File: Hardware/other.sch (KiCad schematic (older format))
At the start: 28 parts, among them J10 TILT_OUT, J11 TILT IN, J12 LED EN, J5 DBG, J6 TRACE, J7 I2C INTERNAL, J8 B5B-XH-A__LF__SN_, J9 B8B-XH-A_LF__SN_

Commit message: Add pcb route and ground plane
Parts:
- removed D8: LED_0805, symbol Device:LED_ALT
- removed J10: TILT_OUT, Connector_PinHeader_2.54mm:PinHeader_1x01_P2.54mm_Vertical, symbol Connector:Conn_01x01_Male
- removed J11: TILT IN, Connector_PinHeader_2.54mm:PinHeader_1x01_P2.54mm_Vertical, symbol Connector:Conn_01x01_Male
- removed R70: 1.5K, Resistor_SMD:R_0603_1608Metric, symbol Device:R
- removed S4: POWER, EcoApi_pcb:SW_PUSH, symbol EcoApi_pcb:SW_PUSH
- added J10: TILT, Connector_PinHeader_2.54mm:PinHeader_1x02_P2.54mm_Vertical, symbol Connector:Conn_01x02_Male
- D7: value LED_0805 -> LED_0603_BLUE; footprint (none) -> LED_SMD:LED_0603_1608Metric
- J12: value LED EN -> POWER ON
- J5: footprint (none) -> Connector_PinHeader_2.54mm:PinHeader_1x05_P2.54mm_Vertical
- J6: footprint (none) -> Connector_PinHeader_2.54mm:PinHeader_1x03_P2.54mm_Vertical
- J8: footprint (none) -> EcoApi_pcb:SHDR5W64P0X250_1X5_1490X575X700P
- J9: footprint (none) -> EcoApi_pcb:SHDR8W64P0X250_1X8_2240X575X700P
- S2: footprint (none) -> EcoApi_pcb:DSHP06TSGET
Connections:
- net labels removed: LOADCELL_E-, LOADCELL_SHIELD
- wire segments 81 -> 82
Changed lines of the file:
@@
 Text GLabel 2600 1350 2    50   Input ~ 0
 LOADCELL_E+
-Text GLabel 2600 1450 2    50   Input ~ 0
-LOADCELL_E-
 Text GLabel 2600 1550 2    50   Input ~ 0
 LOADCELL_A-
@@
 NoConn ~ 1650 4750
 NoConn ~ 1650 4850
-Text GLabel 2600 1750 2    50   Input ~ 0
-LOADCELL_SHIELD
 Text Notes 1100 1750 0    50   ~ 0
 E+ Red\nE- Black\nA- White\nA+ Green / Blue\nSh Yellow
@@
 	1    0    0    -1
 $EndComp
-Wire Wire Line
-	10650 2250 10650 2100
 Text GLabel 10550 1500 0    50   Output ~ 0
 BTN_PWR
-$Comp
-L EcoApi_pcb:SW_PUSH S?
-U 1 1 61E97F11
-P 10650 1800
-AR Path="/61E97F11" Ref="S?"  Part="1"
-AR Path="/62EA3721/61E97F11" Ref="S?"  Part="1"
-AR Path="/61B961C0/61E97F11" Ref="S4"  Part="1"
-AR Path="/62CC297B/61E97F11" Ref="S?"  Part="1"
-F 0 "S4" V 10604 1912 50  0000 L CNN
-F 1 "POWER" V 10695 1912 50  0000 L CNN
-F 2 "EcoApi_pcb:SW_PUSH" H 10650 1800 50  0001 L BNN
-F 3 "" H 10650 1800 50  0001 L BNN
-F 4 "Compliant" H 10650 1800 50  0001 L BNN "EU_RoHS_Compliance"
-F 5 "1571527-1" H 10650 1800 50  0001 L BNN "Comment"
-	1    10650 1800
-	0    1    1    0
-$EndComp
 Wire Wire Line
 	10550 1500 10650 1500
-Connection ~ 10650 1500
 Text GLabel 10550 1000 0    50   Input ~ 0
 VBAT
@@
 Wire Wire Line
 	8150 850  8150 1000
-$Comp
-L Connector:Conn_01x01_Male J?
-U 1 1 61E97F3E
-P 8600 2000
-AR Path="/62CC297B/61E97F3E" Ref="J?"  Part="1"
-AR Path="/61B961C0/61E97F3E" Ref="J10"  Part="1"
-F 0 "J10" H 8708 2181 50  0000 C CNN
-F 1 "TILT_OUT" H 8708 2090 50  0000 C CNN
-F 2 "Connector_PinHeader_2.54mm:PinHeader_1x01_P2.54mm_Vertical" H 8600 2000 50  0001 C CNN
-F 3 "~" H 8600 2000 50  0001 C CNN
-	1    8600 2000
-	-1   0    0    1
-$EndComp
-$Comp
-L Connector:Conn_01x01_Male J?
-U 1 1 61E97F44
-P 8600 2200
-AR Path="/62CC297B/61E97F44" Ref="J?"  Part="1"
-AR Path="/61B961C0/61E97F44" Ref="J11"  Part="1"
-F 0 "J11" H 8708 2381 50  0000 C CNN
-F 1 "TILT IN" H 8708 2290 50  0000 C CNN
-F 2 "Connector_PinHeader_2.54mm:PinHeader_1x01_P2.54mm_Vertical" H 8600 2200 50  0001 C CNN
-F 3 "~" H 8600 2200 50  0001 C CNN
-	1    8600 2200
-	-1   0    0    1
-$EndComp
 $Comp
 L Device:C C?
@@
 Wire Wire Line
 	8400 2000 7900 2000
-Wire Wire Line
-	8400 2200 8400 2500
 Text GLabel 1350 5700 2    50   Output ~ 0
 SW_CLK
@@
 AR Path="/61B961C0/61ED3104" Ref="D7"  Part="1"
 F 0 "D7" H 9150 4100 50  0000 C CNN
-F 1 "LED_0805" H 9150 4200 50  0000 C CNN
-F 2 "" H 9150 3950 50  0001 C CNN
+F 1 "LED_0603_BLUE" H 9150 4200 50  0000 C CNN
+F 2 "LED_SMD:LED_0603_1608Metric" H 9150 3950 50  0001 C CNN
 F 3 "~" H 9150 3950 50  0001 C CNN
 	1    9150 3950
@@
 Text GLabel 9900 3950 2    50   Input ~ 0
 LED_INFO
-$Comp
-L Device:R R?
-U 1 1 61F17383
-P 9400 3150
-AR Path="/61F17383" Ref="R?"  Part="1"
-AR Path="/62CC297B/61F17383" Ref="R?"  Part="1"
-AR Path="/61B961C0/61F17383" Ref="R70"  Part="1"
-F 0 "R70" H 9470 3196 50  0000 L CNN
-F 1 "1.5K" H 9470 3105 50  0000 L CNN
-F 2 "Resistor_SMD:R_0603_1608Metric" V 9330 3150 50  0001 C CNN
-F 3 "~" H 9400 3150 50  0001 C CNN
-	1    9400 3150
-	0    1    1    0
-$EndComp
-$Comp
-L Device:LED_ALT D?
-U 1 1 61F17389
-P 9800 3150
-AR Path="/62CC297B/61F17389" Ref="D?"  Part="1"
-AR Path="/61B961C0/61F17389" Ref="D8"  Part="1"
-F 0 "D8" H 9800 3300 50  0000 C CNN
-F 1 "LED_0805" H 9800 3400 50  0000 C CNN
-F 2 "" H 9800 3150 50  0001 C CNN
-F 3 "~" H 9800 3150 50  0001 C CNN
-	1    9800 3150
-	-1   0    0    1
-$EndComp
-Wire Wire Line
-	9150 3150 9250 3150
-$Comp
-L Connector:Conn_01x02_Male J?
-U 1 1 61F17391
-P 10100 3350
-AR Path="/61F17391" Ref="J?"  Part="1"
-AR Path="/62EA3721/61F17391" Ref="J?"  Part="1"
-AR Path="/61B961C0/61F17391" Ref="J12"  Part="1"
-F 0 "J12" V 10200 3550 50  0000 R CNN
-F 1 "LED EN" V 10000 3600 50  0000 R CNN
-F 2 "Connector_PinHeader_2.54mm:PinHeader_1x02_P2.54mm_Vertical" H 10100 3350 50  0001 C CNN
-F 3 "~" H 10100 3350 50  0001 C CNN
-	1    10100 3350
-	0    -1   -1   0
-$EndComp
-Text GLabel 10350 3150 2    50   Input ~ 0
-LED_INFO
-$Comp
-L EcoApi_pcb-rescue:+3V3-BluePillF4 #SUPPLY?
-U 1 1 61F2426A
-P 9150 3150
-AR Path="/61F2426A" Ref="#SUPPLY?"  Part="1"
-AR Path="/62EA3721/61F2426A" Ref="#SUPPLY?"  Part="1"
-AR Path="/61B961C0/61F2426A" Ref="#SUPPLY0125"  Part="1"
-F 0 "#SUPPLY0125" H 9150 3150 45  0001 L BNN
-F 1 "+3V3" H 9150 3321 45  0000 C CNN
-F 2 "" H 9150 3150 60  0001 C CNN
-F 3 "" H 9150 3150 60  0001 C CNN
-	1    9150 3150
-	0    -1   -1   0
-$EndComp
-Wire Wire Line
-	9550 3150 9650 3150
-Wire Wire Line
-	9950 3150 10100 3150
 Wire Wire Line
 	9400 3950 9300 3950
-Wire Wire Line
-	10200 3150 10350 3150
 $Comp
 L EcoApi_pcb:+3V3-Ext #SUPPLY0126
@@
 Text Notes 7150 6250 0    50   ~ 0
 DSHP06TSGET\n1/12 : boot0 enable\n2/11 : Led info enable\n3/10 : Trace enable\n4/9 : Scale type (full or half)\n5/8 : Wdg delay 1\n6/7 : Wdg delay 2
-Text GLabel 2600 2850 2    50   Output ~ 0
+Text GLabel 2600 2750 2    50   Output ~ 0
 I2S_CK-MIC_GAIN
+Text GLabel 2600 2850 2    50   Input ~ 0
+I2S_WS
 Text GLabel 2600 2950 2    50   Input ~ 0
-I2S_WS
-Text GLabel 2600 2750 2    50   Input ~ 0
 I2S_SD-MIC_ANA
 $Comp
@@
 F 0 "S2" H 8050 4765 50  0000 C CNN
 F 1 "DSHP06TSGET" H 8050 4674 50  0000 C CNN
-F 2 "" H 8500 4600 50  0001 L CNN
+F 2 "EcoApi_pcb:DSHP06TSGET" H 8500 4600 50  0001 L CNN
 F 3 "https://datasheet.lcsc.com/szlcsc/1810191313_Dongguan-Guangzhu-Industrial-DSHP06TSGET_C40737.pdf" H 8500 4500 50  0001 L CNN
 F 4 "SPST 6 1.27mm, Half Slide (Standard) Black SMD DIP Switches" H 8500 4400 50  0001 L CNN "Description"
@@
 F 0 "J5" H 1258 5981 50  0000 C CNN
 F 1 "DBG" H 1258 5890 50  0000 C CNN
-F 2 "" H 1150 5600 50  0001 C CNN
+F 2 "Connector_PinHeader_2.54mm:PinHeader_1x05_P2.54mm_Vertical" H 1150 5600 50  0001 C CNN
 F 3 "~" H 1150 5600 50  0001 C CNN
 	1    1150 5600
@@
 F 0 "J6" H 1258 6731 50  0000 C CNN
 F 1 "TRACE" H 1258 6640 50  0000 C CNN
-F 2 "" H 1150 6450 50  0001 C CNN
+F 2 "Connector_PinHeader_2.54mm:PinHeader_1x03_P2.54mm_Vertical" H 1150 6450 50  0001 C CNN
 F 3 "~" H 1150 6450 50  0001 C CNN
 	1    1150 6450
@@
 F 0 "J8" H 2892 1085 50  0000 C CNN
 F 1 "B5B-XH-A__LF__SN_" H 2892 1176 50  0000 C CNN
-F 2 "" H 3250 1850 50  0001 L CNN
+F 2 "EcoApi_pcb:SHDR5W64P0X250_1X5_1490X575X700P" H 3250 1850 50  0001 L CNN
 F 3 "http://www.farnell.com/datasheets/1684882.pdf" H 3250 1750 50  0001 L CNN
 F 4 "Shrouded hdr,XH,2.5mm pitch,straight,5w JST XH Series, 2.5mm Pitch 5 Way 1 Row Straight PCB Header, Solder Termination, 3A" H 3250 1650 50  0001 L CNN "Description"
@@
 F 0 "J9" H 2892 2385 50  0000 C CNN
 F 1 "B8B-XH-A_LF__SN_" H 2892 2476 50  0000 C CNN
-F 2 "" H 3250 3450 50  0001 L CNN
+F 2 "EcoApi_pcb:SHDR8W64P0X250_1X8_2240X575X700P" H 3250 3450 50  0001 L CNN
 F 3 "https://datasheet.datasheetarchive.com/originals/distributors/Datasheets_SAMA/45bda73f655da0a850bf2ea3e93b2e86.pdf" H 3250 3350 50  0001 L CNN
 F 4 "XH-2.5mm Header top entry 8 way JST XH Series, Series Number B8B, 2.5mm Pitch 8 Way 1 Row Straight PCB Header, Solder Termination, 3A" H 3250 3250 50  0001 L CNN "Description"
@@
 Wire Wire Line
 	6550 850  6550 1000
+$Comp
+L Connector:Conn_01x02_Male J?
+U 1 1 63C32D33
+P 10850 1800
+AR Path="/63C32D33" Ref="J?"  Part="1"
+AR Path="/62D38F6A/63C32D33" Ref="J?"  Part="1"
+AR Path="/62CC297B/63C32D33" Ref="J?"  Part="1"
+AR Path="/61B961C0/63C32D33" Ref="J12"  Part="1"
+F 0 "J12" V 10950 2000 50  0000 R CNN
+F 1 "POWER ON" V 10750 2050 50  0000 R CNN
+F 2 "Connector_PinHeader_2.54mm:PinHeader_1x02_P2.54mm_Vertical" H 10850 1800 50  0001 C CNN
+F 3 "~" H 10850 1800 50  0001 C CNN
+	1    10850 1800
+	-1   0    0    1
+$EndComp
+Wire Wire Line
+	10650 1800 10650 2250
+Wire Wire Line
+	10650 1500 10650 1700
+Connection ~ 10650 1500
+$Comp
+L Connector:Conn_01x02_Male J?
+U 1 1 63DDD3C1
+P 8600 2100
+AR Path="/63DDD3C1" Ref="J?"  Part="1"
+AR Path="/62D38F6A/63DDD3C1" Ref="J?"  Part="1"
+AR Path="/62CC297B/63DDD3C1" Ref="J?"  Part="1"
+AR Path="/61B961C0/63DDD3C1" Ref="J10"  Part="1"
+F 0 "J10" V 8700 2300 50  0000 R CNN
+F 1 "TILT" V 8500 2350 50  0000 R CNN
+F 2 "Connector_PinHeader_2.54mm:PinHeader_1x02_P2.54mm_Vertical" H 8600 2100 50  0001 C CNN
+F 3 "~" H 8600 2100 50  0001 C CNN
+	1    8600 2100
+	-1   0    0    1
+$EndComp
+Wire Wire Line
+	8400 2100 8400 2500
+$Comp
+L power:GND #PWR?
+U 1 1 63E19E1A
+P 3250 1800
+AR Path="/63E19E1A" Ref="#PWR?"  Part="1"
+AR Path="/62D38F6A/63E19E1A" Ref="#PWR?"  Part="1"
+AR Path="/62EA3721/63E19E1A" Ref="#PWR?"  Part="1"
+AR Path="/61B961C0/63E19E1A" Ref="#PWR0188"  Part="1"
+F 0 "#PWR0188" H 3250 1550 50  0001 C CNN
+F 1 "GND" H 3255 1627 50  0000 C CNN
+F 2 "" H 3250 1800 50  0001 C CNN
+F 3 "" H 3250 1800 50  0001 C CNN
+	1    3250 1800
+	1    0    0    -1
+$EndComp
+Wire Wire Line
+	2600 1750 3250 1750
+Wire Wire Line
+	3250 1750 3250 1800
+Wire Wire Line
+	2600 1450 3250 1450
+Wire Wire Line
+	3250 1450 3250 1750
+Connection ~ 3250 1750
 $EndSCHEMATC

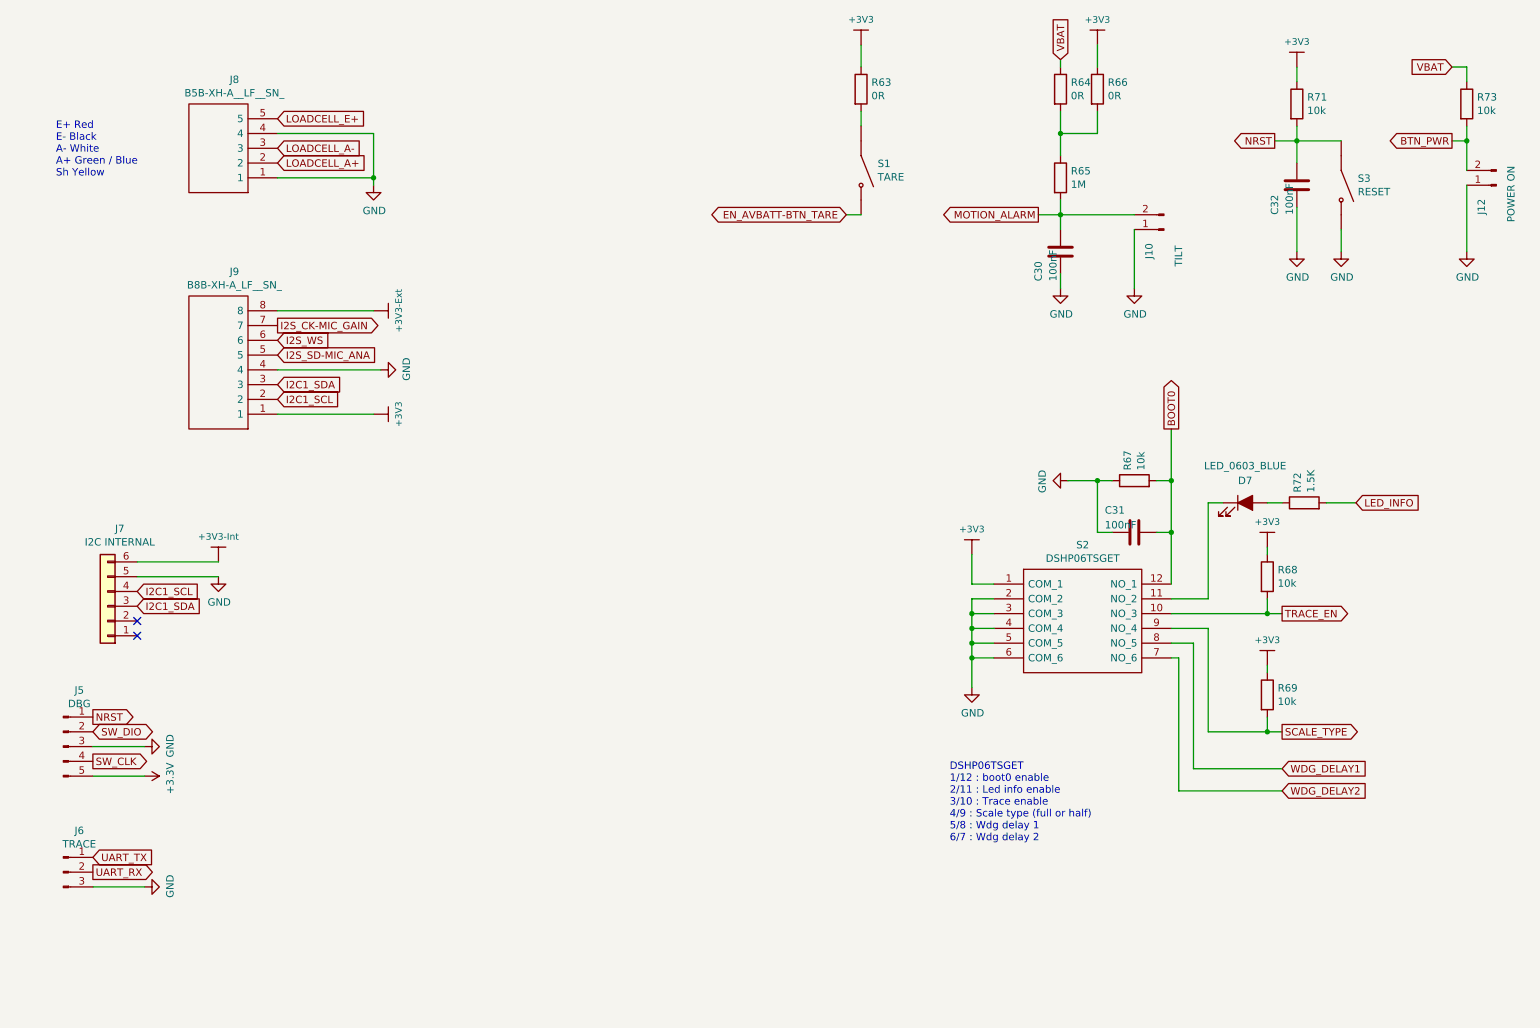
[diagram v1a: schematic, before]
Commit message: Update pcb to v2.1 (Add ldo)
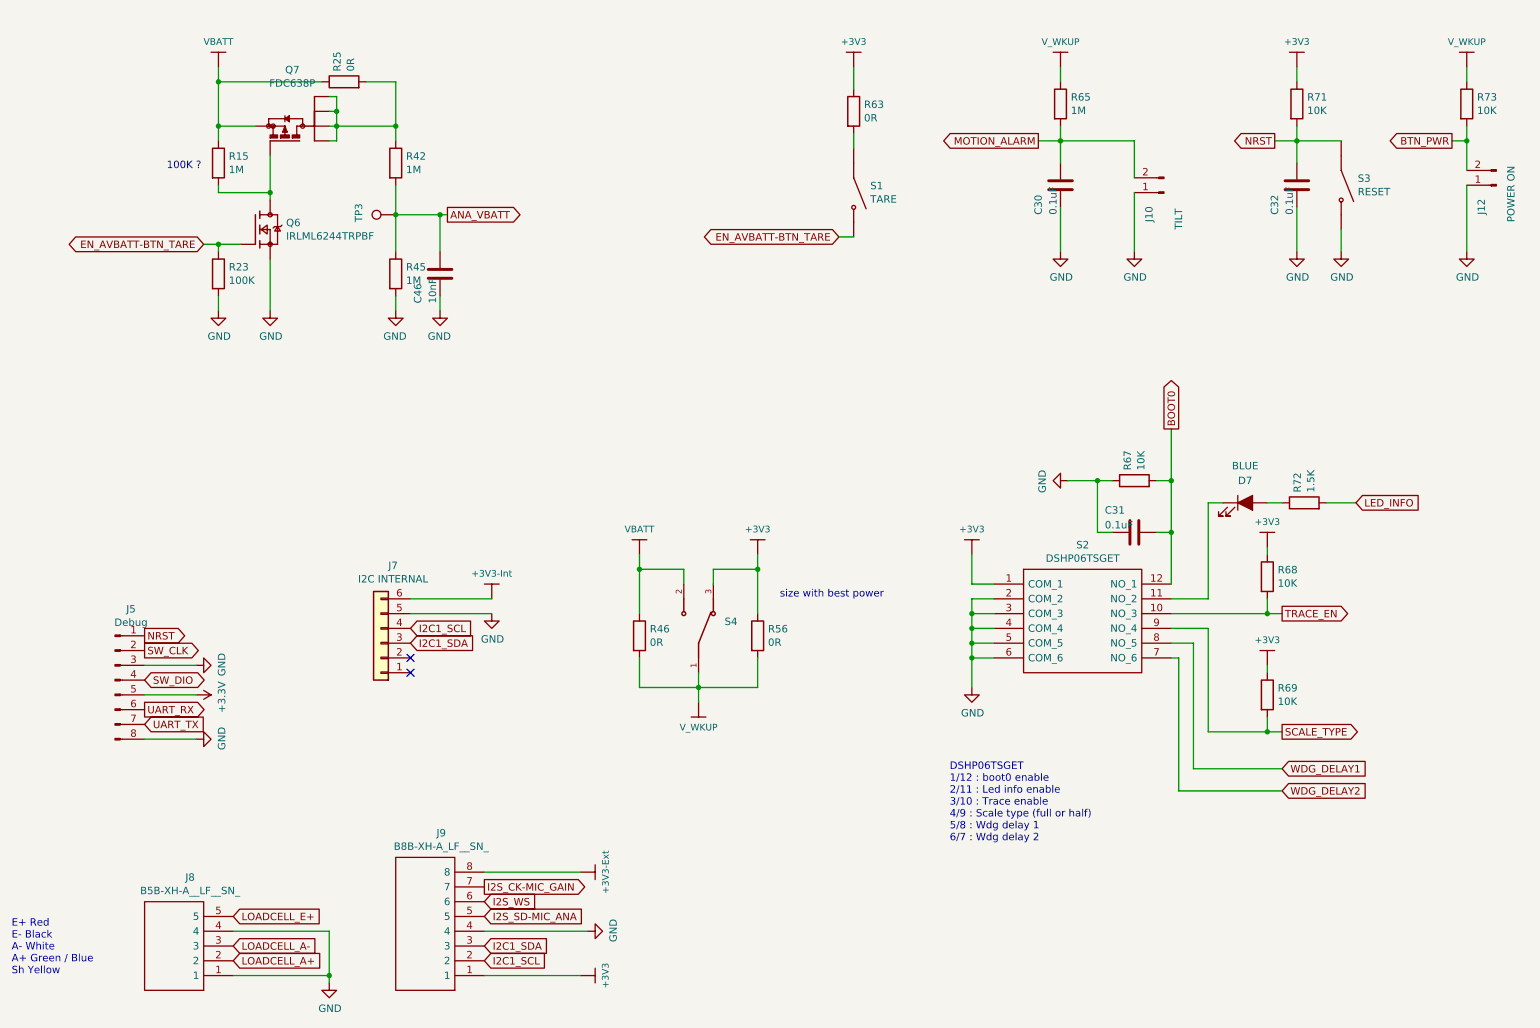
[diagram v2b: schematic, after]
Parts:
- removed J5: DBG, Connector_PinHeader_2.54mm:PinHeader_1x05_P2.54mm_Vertical, symbol Connector:Conn_01x05_Male
- removed J6: TRACE, Connector_PinHeader_2.54mm:PinHeader_1x03_P2.54mm_Vertical, symbol Connector:Conn_01x03_Male
- removed R64, R66: 0R, Resistor_SMD:R_0603_1608Metric, symbol Device:R
- added C46: 10nF, Capacitor_SMD:C_0603_1608Metric, symbol Device:C
- added J5: Debug, Connector_PinHeader_2.54mm:PinHeader_1x08_P2.54mm_Vertical, symbol Connector:Conn_01x08_Male
- added Q6: IRLML6244TRPBF, EcoApi_pcb:SOT95P237X112-3N, symbol EcoApi_pcb:IRLML6244TRPBF
- added Q7: FDC638P, EcoApi_pcb:SSOT-6, symbol EcoApi_pcb:FDC638P
- added R15, R42, R45: 1M, Resistor_SMD:R_0603_1608Metric, symbol Device:R
- added R23: 100K, Resistor_SMD:R_0603_1608Metric, symbol Device:R
- added R25: 0R, Resistor_SMD:R_0603_1608Metric, symbol Device:R
- added R46, R56: 0R, Resistor_SMD:R_1206_3216Metric, symbol Device:R
- added S4: MSS-102559-14A-D, EcoApi_pcb:SW_MSS-102559-14A-D, symbol EcoApi_pcb:MSS-102559-14A-D
- added TP3: TestPoint, TestPoint:TestPoint_Pad_D1.0mm, symbol Connector:TestPoint
- C30, C31, C32: value 100nF -> 0.1uF; Populate (none) -> yes; Size Inch (none) -> 0603; Size Metric (none) -> 1608
- D7: value LED_0603_BLUE -> BLUE; Populate (none) -> yes; Size Inch (none) -> 0603; Size Metric (none) -> 1608
- J10, J12, J7, J8, J9, S1, S3: Populate (none) -> no
- R63, R65, R72: Populate (none) -> yes; Size Inch (none) -> 0603; Size Metric (none) -> 1608; Tolerance (none) -> 1%
- R67, R68, R69, R71, R73: value 10k -> 10K; Populate (none) -> yes; Size Inch (none) -> 0603; Size Metric (none) -> 1608; Tolerance (none) -> 1%
- S2: Populate (none) -> yes
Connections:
- net VBAT is gone; now on net V_WKUP: R73.1
- net +3V3: now also J5.5 (Pin_5), R56.1, S4.3
- net EN_AVBATT-BTN_TARE: now also Q6.1, R23.1
- net GND: now also C46.2, J5.3 (Pin_3), J5.8 (Pin_8), Q6.2, R23.2, R45.2
- net NRST: now also J5.1 (Pin_1)
- net SW_CLK: now also J5.2 (Pin_2)
- net SW_DIO: now also J5.4 (Pin_4)
- net UART_RX: now also J5.6 (Pin_6)
- net UART_TX: now also J5.7 (Pin_7)
- net V_WKUP: now reaches R65.1
- net V_WKUP: now also R46.2, R56.2, S4.1
- new net: Q7.1, Q7.2, Q7.5, Q7.6, R25.2, R42.1
- new net: Q6.3, Q7.3, R15.2
- new net ANA_VBATT: C46.1, R42.2, R45.1, TP3.1
- new net VBATT: Q7.4, R15.1, R25.1, R46.1, S4.2
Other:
- note added: "100K ?"
- note added: "size with best power"
- moved on the sheet: C30, J10, J7, J8, J9, R63, R65, S1
